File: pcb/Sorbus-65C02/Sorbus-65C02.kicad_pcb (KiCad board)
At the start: 2 copper layers, 83.8 x 48.3 mm, 9 parts, among them J1 Conn_01x32_Pin, U1 W65C02SxP

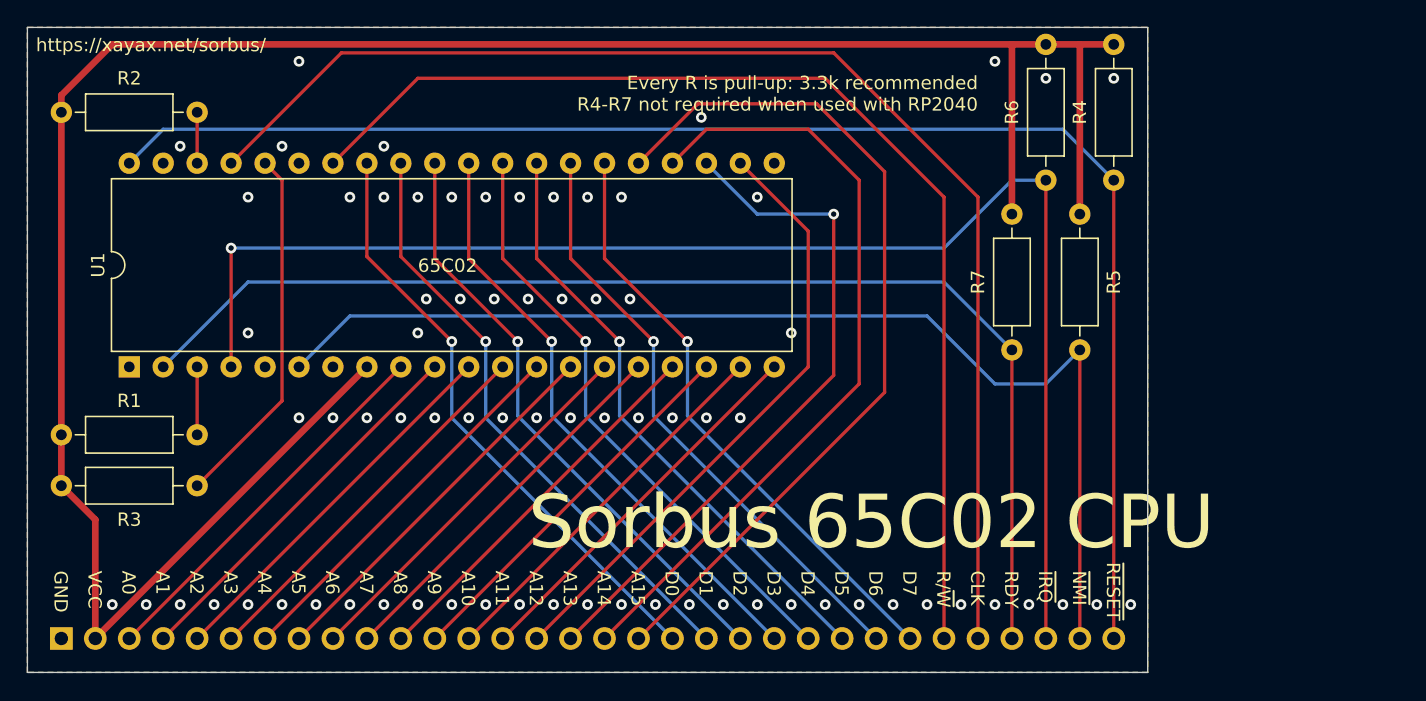
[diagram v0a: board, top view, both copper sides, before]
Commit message: updated PCB design - added decoupling capacitor to 65C02 board - replaced simple connectors with real RP2040 Purple component - also updated gerber file and PDF exports from PCB changes - fixed problem in bare build
Signed-off-by: Sven Oliver Moll <svolli@svolli.de>
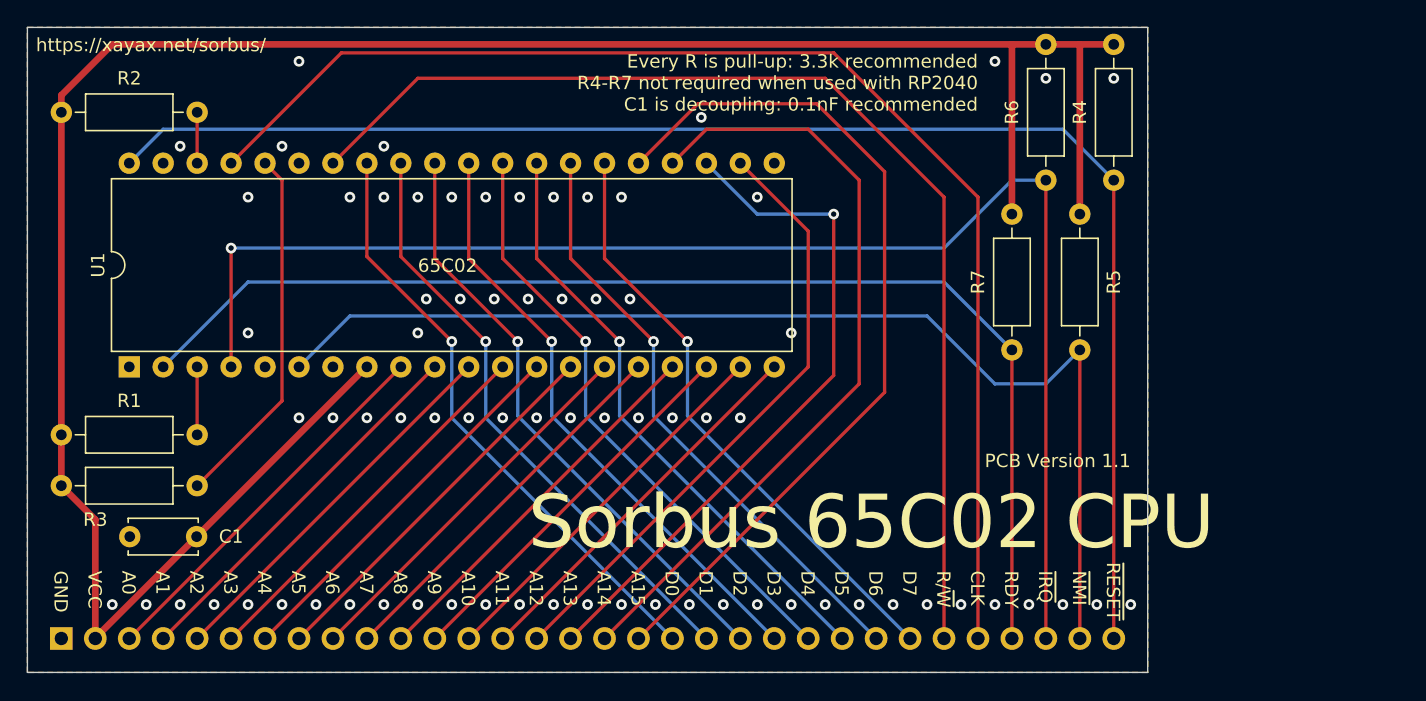
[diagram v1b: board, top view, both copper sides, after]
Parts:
- added C1: C, Capacitor_THT:C_Disc_D5.0mm_W2.5mm_P5.00mm, F.Cu at (33.1, 73.7)
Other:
- board text added: "Every R is pull-up: 3.3k recommended R4-R7 not required when used with RP2040 C1 is decoupling: 0.1nF recommended"
- board text added: "PCB Version 1.1"
- board text removed: "Every R is pull-up: 3.3k recommended R4-R7 not required when used with RP2040"
